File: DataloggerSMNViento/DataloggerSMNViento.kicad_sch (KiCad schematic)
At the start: 0 parts

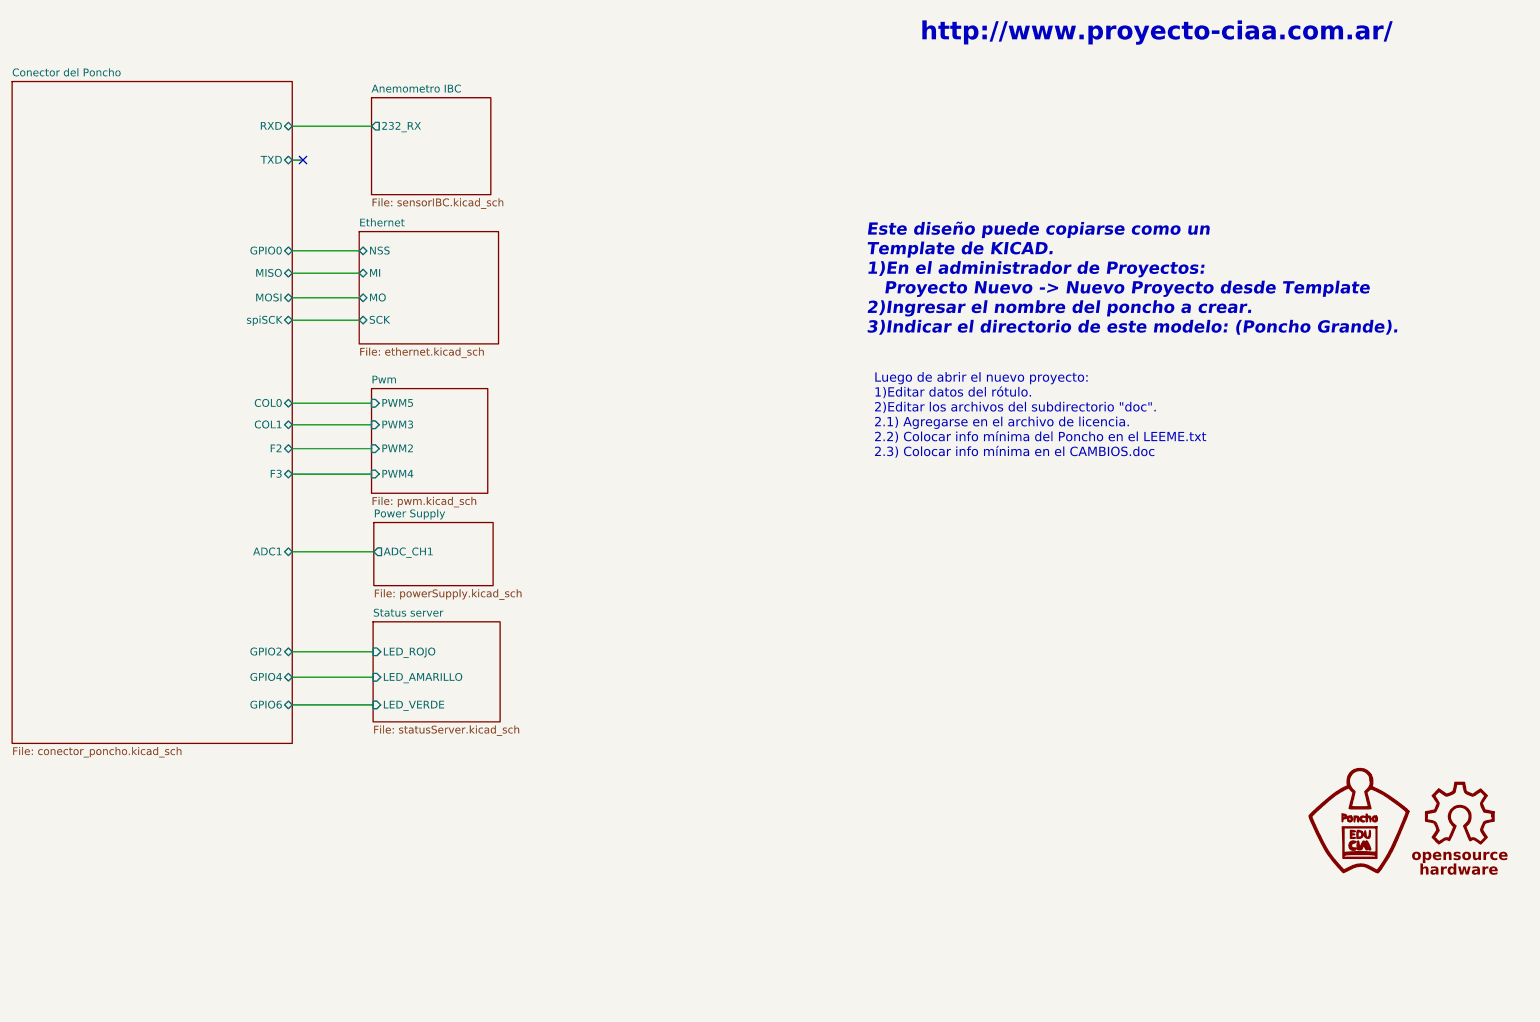
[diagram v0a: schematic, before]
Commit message: Agrego modificaciones al poncho de la EDU CIAA, también agrego una simulacion del circuito para tomar la tensión del ADC del tunnel
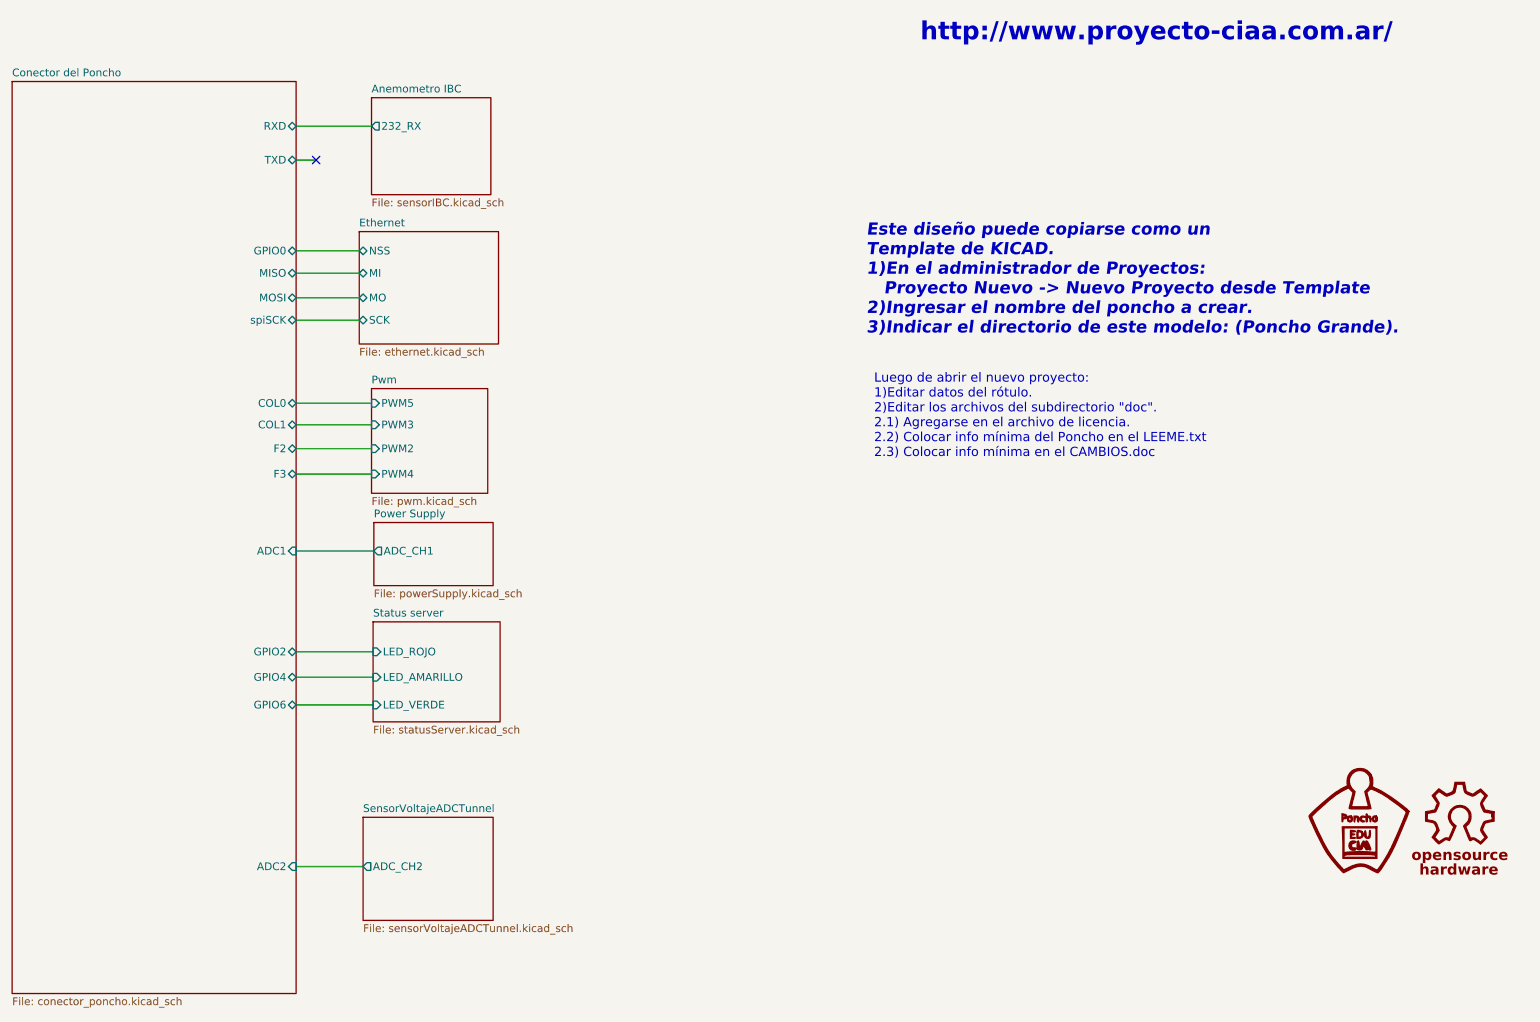
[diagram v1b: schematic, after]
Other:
- added sheet SensorVoltajeADCTunnel (sensorVoltajeADCTunnel.kicad_sch)
- sheet Conector del Poncho ports: added ADC2; removed none
- company: Proyecto CIAA - COMPUTADORA INDUSTRIAL ABIERTA ARGENTINA -> Servicio Meteorológico Nacional - FIUBA - UBA
- title: Poncho Grande - Modelo - Ejemplo - Template -> Datalogger para SCTV
